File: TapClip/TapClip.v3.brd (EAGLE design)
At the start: 54.6 x 38.1 mm, 22 parts, among them J1 AVR_SPI_PRG_6PTH

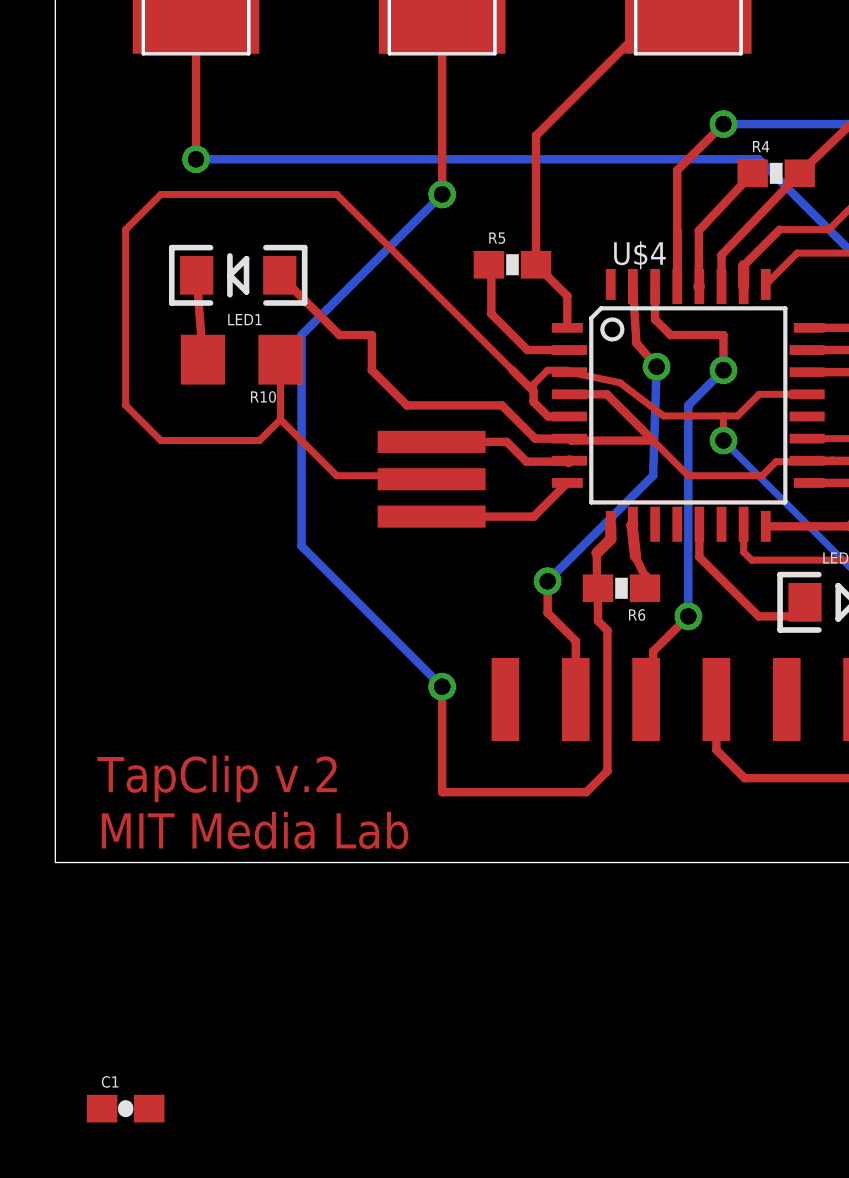
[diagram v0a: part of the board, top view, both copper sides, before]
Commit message: Adding board w/ sound.
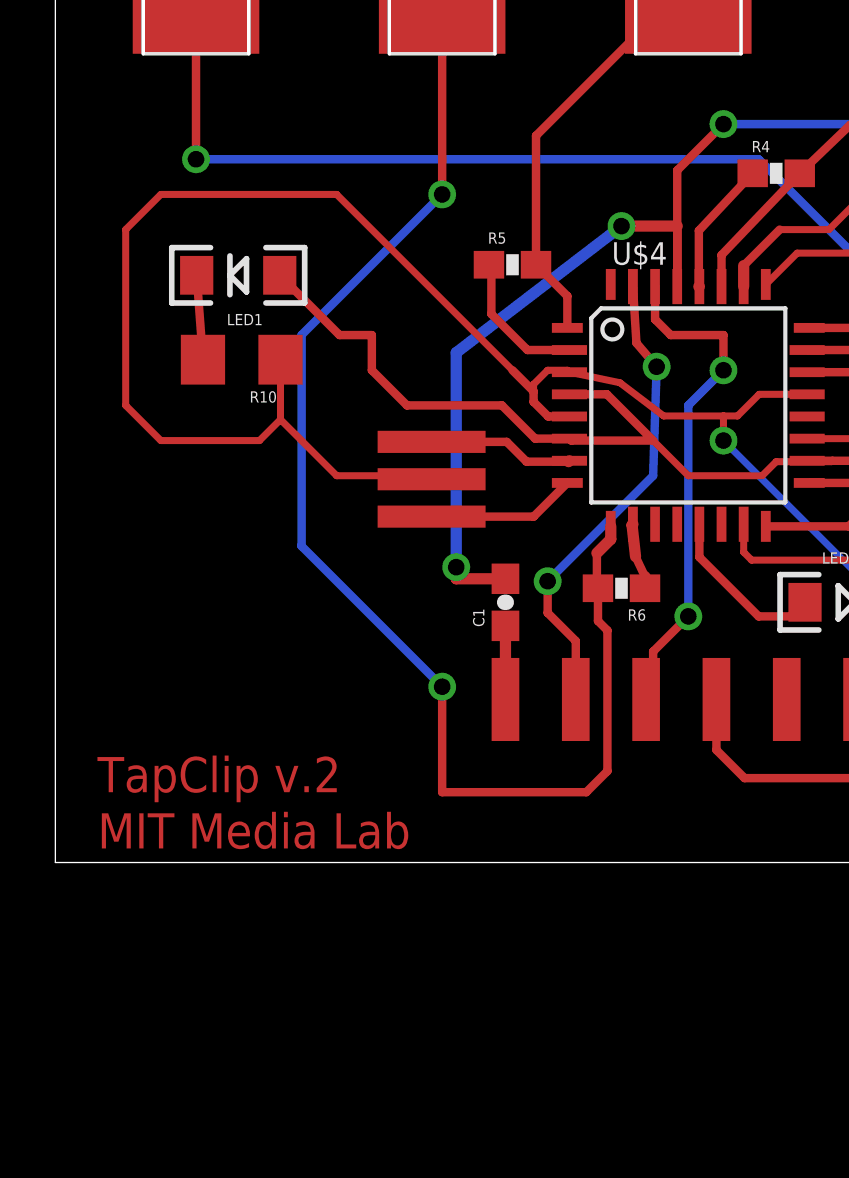
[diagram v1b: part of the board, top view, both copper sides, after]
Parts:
- moved C1 22.9 mm to (39.1, 6.86), turned to 90 degrees
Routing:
- net RST: track 66.2 -> 85.7 mm, vias 2 -> 4
- net DTR: track 0.00 -> 2.66 mm
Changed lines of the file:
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@@
 <element name="R7" library="SparkFun" package="0603-RES" value="" x="54.102" y="14.859"/>
 <element name="J1" library="SparkFun" package="2X3" value="AVR_SPI_PRG_6PTH" x="64.77" y="12.7" rot="R270"/>
-<element name="C1" library="SparkFun" package="0603-CAP" value="" x="25.4" y="-11.43"/>
+<element name="C1" library="SparkFun" package="0603-CAP" value="" x="39.116" y="6.858" rot="R90"/>
 </elements>
 <signals>
@@
 <contactref element="U$4" pad="29"/>
 <wire x1="45.32" y1="18.2626" x2="45.32" y2="20.3" width="0.3048" layer="1"/>
-<wire x1="45.32" y1="18.2626" x2="45.32" y2="22.46" width="0.3048" layer="1"/>
+<wire x1="45.32" y1="18.2626" x2="45.32" y2="20.447" width="0.3048" layer="1"/>
+<wire x1="45.32" y1="20.447" x2="45.32" y2="22.46" width="0.3048" layer="1"/>
 <wire x1="45.32" y1="22.46" x2="46.99" y2="24.13" width="0.3048" layer="1"/>
 <via x="46.99" y="24.13" extent="1-16" drill="0.6" shape="square"/>
@@
 <wire x1="62.23" y1="3.81" x2="67.31" y2="3.81" width="0.254" layer="16"/>
 <contactref element="C1" pad="2"/>
-<wire x1="26.25" y1="-11.43" x2="45.32" y2="18.2626" width="0" layer="19" extent="1-1"/>
+<wire x1="39.116" y1="7.708" x2="37.338" y2="7.708" width="0.4064" layer="1"/>
+<wire x1="37.338" y1="7.708" x2="37.338" y2="8.128" width="0.4064" layer="1"/>
+<via x="37.338" y="8.128" extent="1-16" drill="0.6" shape="square"/>
+<wire x1="37.338" y1="8.128" x2="37.338" y2="15.875" width="0.4064" layer="16"/>
+<wire x1="37.338" y1="15.875" x2="43.307" y2="20.447" width="0.4064" layer="16"/>
+<via x="43.307" y="20.447" extent="1-16" drill="0.6" shape="square"/>
+<wire x1="43.307" y1="20.447" x2="45.32" y2="20.447" width="0.4064" layer="1"/>
 </signal>
 <signal name="MOSI">
@@
 <contactref element="JP1" pad="1"/>
 <contactref element="C1" pad="1"/>
-<wire x1="24.55" y1="-11.43" x2="39.116" y2="3.349" width="0" layer="19" extent="1-1"/>
+<wire x1="39.116" y1="3.349" x2="39.116" y2="6.008" width="0.4064" layer="1"/>
 </signal>
 <signal name="N$9">
